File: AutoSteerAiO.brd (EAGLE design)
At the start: 114.3 x 99.1 mm, 84 parts, among them IC2 MMA8452Q, J4 CONNECTOR 1x5 PINS, K4 CB1A-P-12V, U1 VX7805-1000

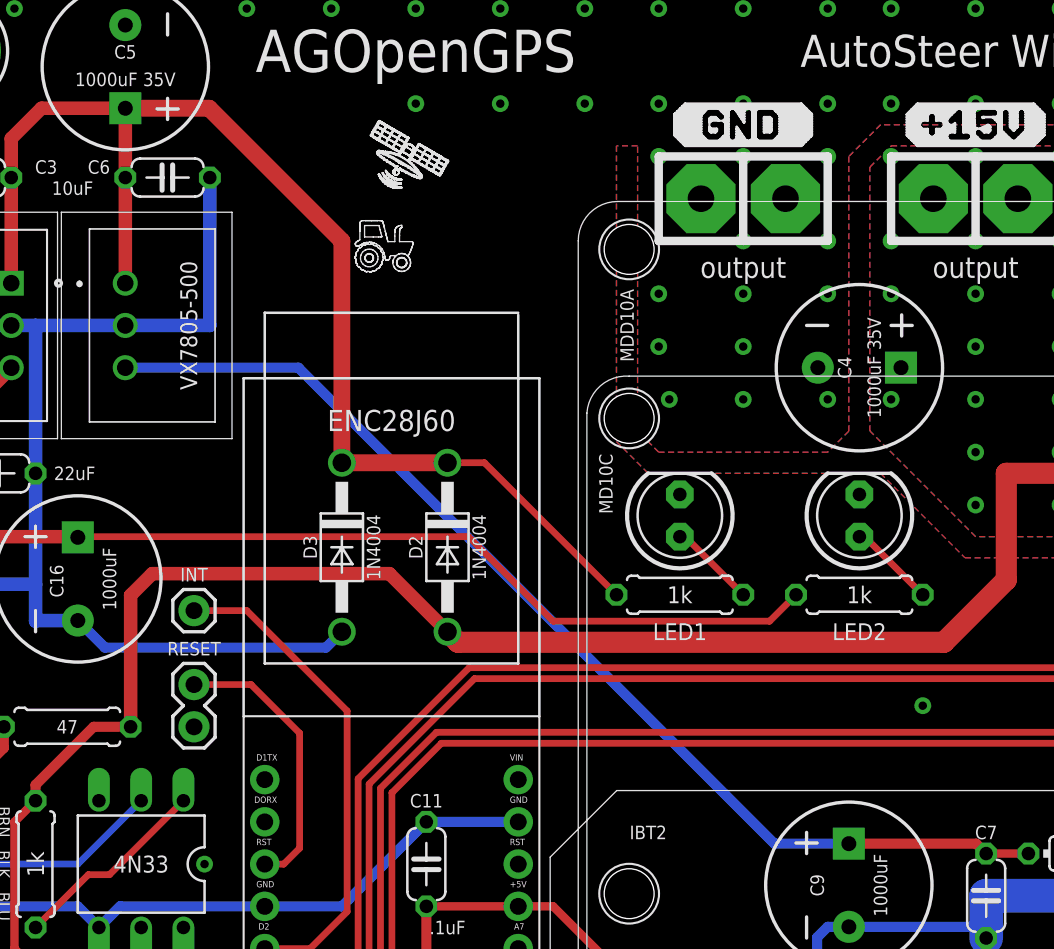
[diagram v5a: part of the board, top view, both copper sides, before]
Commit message: Add files via upload
previous version, wrong footprint VX7805-1000 it can fit, but will come out from PCB.
now it's fixed
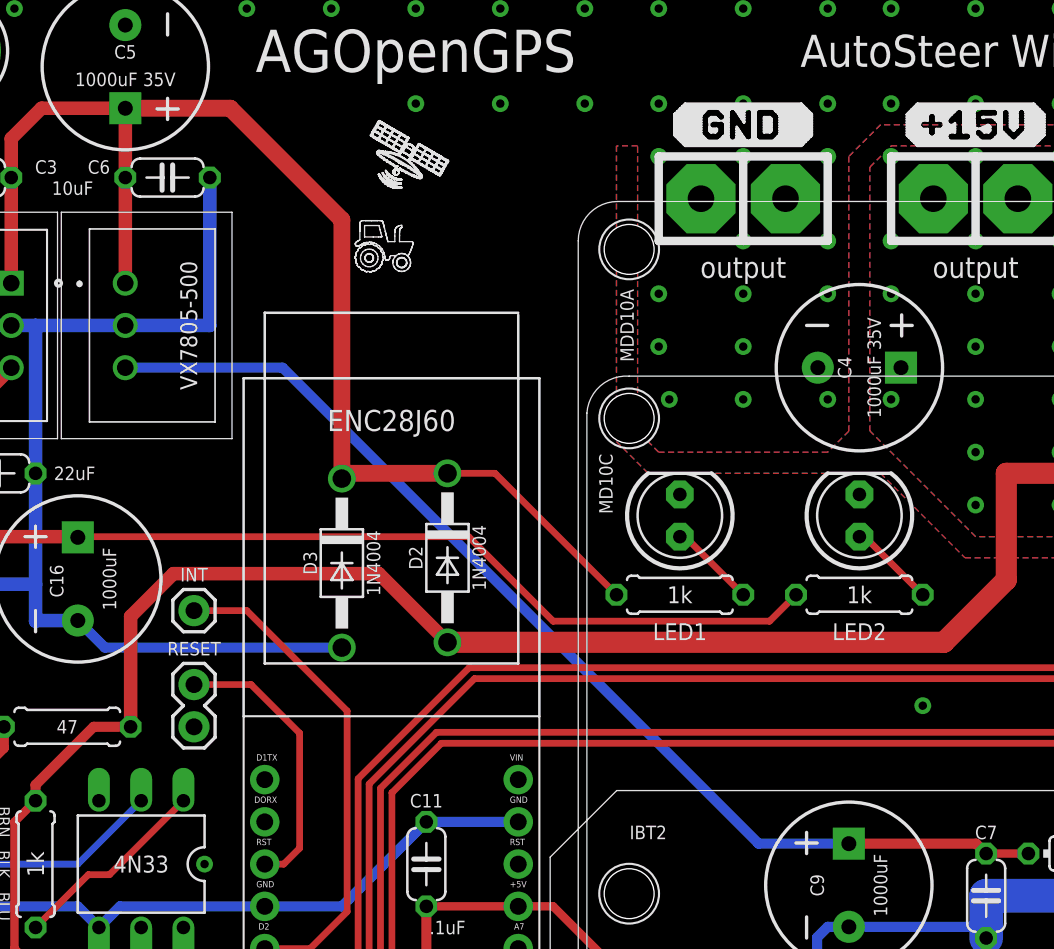
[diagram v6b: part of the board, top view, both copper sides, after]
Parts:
- moved D3 0.95 mm to (28.6, 63.2)
- moved D2 0.64 mm to (34.9, 63.5)
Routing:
- net N$26: track 76.3 -> 77.9 mm
- net +15V: track 121.6 -> 120.9 mm
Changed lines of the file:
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@@
 <?xml version="1.0" encoding="utf-8"?>
 <!DOCTYPE eagle SYSTEM "eagle.dtd">
-<eagle version="9.3.1">
+<eagle version="9.3.2">
 <drawing>
 <settings>
@@
 <attribute name="CYTRON-PC" value="CN-2600PS-05" x="109.855" y="48.26" size="1.778" layer="27" rot="R90" display="off"/>
 <attribute name="DESC" value="2600 PCB Connector" x="109.855" y="48.26" size="1.778" layer="27" rot="R90" display="off"/>
-<attribute name="LABEL" value="" x="112.776" y="46.863" size="0.762" layer="21" font="vector" ratio="15" rot="R90" align="top-left"/>
 <attribute name="LABEL" value="" x="112.776" y="46.863" size="0.762" layer="51" font="vector" ratio="15" rot="R90" align="top-left"/>
+<attribute name="LABEL" value="" x="112.776" y="46.863" size="0.762" layer="21" font="vector" ratio="15" rot="R90" align="top-left"/>
 <attribute name="LABEL" value="" x="109.855" y="48.26" size="1.778" layer="27" rot="R90" display="off"/>
 <attribute name="MF" value="" x="109.855" y="48.26" size="1.778" layer="27" rot="R90" display="off"/>
@@
 <attribute name="VALUE" x="16.51" y="6.985" size="1.016" layer="25" font="vector" ratio="12" rot="R180" align="center"/>
 </element>
-<element name="D2" library="diode" library_urn="urn:adsk.eagle:library:210" package="DO41-10" package3d_urn="urn:adsk.eagle:package:43336/1" value="1N4004" x="34.925" y="64.135" smashed="yes" rot="R270">
-<attribute name="MF" value="" x="34.925" y="64.135" size="1.778" layer="27" rot="R270" display="off"/>
-<attribute name="MPN" value="" x="34.925" y="64.135" size="1.778" layer="27" rot="R270" display="off"/>
-<attribute name="NAME" x="33.02" y="64.135" size="0.8128" layer="25" font="vector" ratio="12" rot="R90" align="center"/>
-<attribute name="OC_NEWARK" value="unknown" x="34.925" y="64.135" size="1.778" layer="27" rot="R270" display="off"/>
-<attribute name="VALUE" x="36.83" y="64.135" size="0.8128" layer="25" font="vector" ratio="12" rot="R90" align="center"/>
-</element>
-<element name="D3" library="diode" library_urn="urn:adsk.eagle:library:210" package="DO41-10" package3d_urn="urn:adsk.eagle:package:43336/1" value="1N4004" x="28.575" y="64.135" smashed="yes" rot="R270">
-<attribute name="MF" value="" x="28.575" y="64.135" size="1.778" layer="27" rot="R270" display="off"/>
-<attribute name="MPN" value="" x="28.575" y="64.135" size="1.778" layer="27" rot="R270" display="off"/>
-<attribute name="NAME" x="26.67" y="64.135" size="0.8128" layer="25" font="vector" ratio="12" rot="R270" align="center"/>
-<attribute name="OC_NEWARK" value="unknown" x="28.575" y="64.135" size="1.778" layer="27" rot="R270" display="off"/>
-<attribute name="VALUE" x="30.48" y="64.135" size="0.8128" layer="25" font="vector" ratio="12" rot="R270" align="center"/>
+<element name="D2" library="diode" library_urn="urn:adsk.eagle:library:210" package="DO41-10" package3d_urn="urn:adsk.eagle:package:43336/1" value="1N4004" x="34.925" y="63.5" smashed="yes" rot="R270">
+<attribute name="MF" value="" x="34.925" y="63.5" size="1.778" layer="27" rot="R270" display="off"/>
+<attribute name="MPN" value="" x="34.925" y="63.5" size="1.778" layer="27" rot="R270" display="off"/>
+<attribute name="NAME" x="33.02" y="63.5" size="0.8128" layer="25" font="vector" ratio="12" rot="R90" align="center"/>
+<attribute name="OC_NEWARK" value="unknown" x="34.925" y="63.5" size="1.778" layer="27" rot="R270" display="off"/>
+<attribute name="VALUE" x="36.83" y="63.5" size="0.8128" layer="25" font="vector" ratio="12" rot="R90" align="center"/>
+</element>
+<element name="D3" library="diode" library_urn="urn:adsk.eagle:library:210" package="DO41-10" package3d_urn="urn:adsk.eagle:package:43336/1" value="1N4004" x="28.575" y="63.1825" smashed="yes" rot="R270">
+<attribute name="MF" value="" x="28.575" y="63.1825" size="1.778" layer="27" rot="R270" display="off"/>
+<attribute name="MPN" value="" x="28.575" y="63.1825" size="1.778" layer="27" rot="R270" display="off"/>
+<attribute name="NAME" x="26.67" y="63.1825" size="0.8128" layer="25" font="vector" ratio="12" rot="R270" align="center"/>
+<attribute name="OC_NEWARK" value="unknown" x="28.575" y="63.1825" size="1.778" layer="27" rot="R270" display="off"/>
+<attribute name="VALUE" x="30.48" y="63.1825" size="0.8128" layer="25" font="vector" ratio="12" rot="R270" align="center"/>
 </element>
 <element name="R4" library="resistor" library_urn="urn:adsk.eagle:library:348" package="0207/7" package3d_urn="urn:adsk.eagle:package:23493/2" value="330" x="96.52" y="20.955" smashed="yes" rot="R180">
@@
 <via x="105.41" y="2.54" extent="1-16" drill="0.508"/>
 <via x="33.02" y="90.805" extent="1-16" drill="0.508"/>
-<wire x1="28.575" y1="59.055" x2="27.6225" y2="58.1025" width="0.6096" layer="16"/>
-<wire x1="27.6225" y1="58.1025" x2="14.3275" y2="58.1025" width="0.6096" layer="16"/>
+<wire x1="28.575" y1="58.1025" x2="14.3275" y2="58.1025" width="0.6096" layer="16"/>
 <wire x1="12.7" y1="59.73" x2="14.3275" y2="58.1025" width="0.6096" layer="16"/>
 <polygon width="0" layer="1" isolate="0.3556" thermals="no" rank="2">
@@
 <wire x1="8.89" y1="40.005" x2="8.89" y2="47.625" width="0.508" layer="1"/>
 <wire x1="8.89" y1="47.625" x2="10.16" y2="48.895" width="0.508" layer="1"/>
-<wire x1="34.925" y1="59.055" x2="31.4325" y2="62.5475" width="0.8128" layer="1"/>
-<wire x1="31.4325" y1="62.5475" x2="17.1763125" y2="62.5475" width="0.8128" layer="1"/>
-<wire x1="17.1763125" y1="62.5475" x2="15.875" y2="61.2461875" width="0.8128" layer="1"/>
+<wire x1="34.925" y1="58.42" x2="30.7975" y2="62.5475" width="0.8128" layer="1"/>
+<wire x1="30.7975" y1="62.5475" x2="18.4463125" y2="62.5475" width="0.8128" layer="1"/>
+<wire x1="18.4463125" y1="62.5475" x2="15.875" y2="59.9761875" width="0.8128" layer="1"/>
 <polygon width="0" layer="16" thermals="no">
 <vertex x="66.675" y="64.77"/>
@@
 <vertex x="79.375" y="64.77"/>
 </polygon>
-<wire x1="15.875" y1="61.2461875" x2="15.875" y2="53.34" width="0.8128" layer="1"/>
+<wire x1="15.875" y1="59.9761875" x2="15.875" y2="53.34" width="0.8128" layer="1"/>
 <wire x1="15.875" y1="53.34" x2="13.6525" y2="53.34" width="0.6096" layer="1"/>
 <wire x1="13.6525" y1="53.34" x2="10.16" y2="49.8475" width="0.6096" layer="1"/>
@@
 <via x="71.755" y="66.675" extent="1-16" drill="0.508"/>
 <via x="75.565" y="66.675" extent="1-16" drill="0.508"/>
-<wire x1="64.77" y1="58.42" x2="35.56" y2="58.42" width="1.27" layer="1"/>
-<wire x1="35.56" y1="58.42" x2="35.179" y2="58.801" width="1.27" layer="1"/>
-<wire x1="35.179" y1="58.801" x2="34.925" y2="59.055" width="1.27" layer="1"/>
+<wire x1="64.77" y1="58.42" x2="34.925" y2="58.42" width="1.27" layer="1"/>
 <wire x1="78.68" y1="68.58" x2="68.52" y2="68.58" width="1.27" layer="1"/>
 <wire x1="68.52" y1="68.58" x2="68.52" y2="62.17" width="1.27" layer="1"/>
@@
 <wire x1="15.5575" y1="80.01" x2="15.555" y2="80.0125" width="0.8128" layer="1"/>
 <wire x1="15.555" y1="80.0125" x2="15.5525" y2="80.01" width="0.8128" layer="1"/>
-<wire x1="34.925" y1="69.215" x2="37.1475" y2="69.215" width="0.4064" layer="1"/>
-<wire x1="45.085" y1="61.2775" x2="37.1475" y2="69.215" width="0.4064" layer="1"/>
+<wire x1="34.925" y1="68.58" x2="37.7825" y2="68.58" width="0.4064" layer="1"/>
+<wire x1="45.085" y1="61.2775" x2="37.7825" y2="68.58" width="0.4064" layer="1"/>
 <wire x1="15.5575" y1="90.5275" x2="15.5575" y2="86.36" width="0.8128" layer="1"/>
 <contactref element="U1" pad="1"/>
@@
 <wire x1="8.6995" y1="86.36" x2="8.7" y2="86.3595" width="0.8128" layer="1"/>
 <wire x1="8.7" y1="86.3595" x2="8.7" y2="80.01" width="0.8128" layer="1"/>
-<wire x1="34.925" y1="69.215" x2="28.575" y2="69.215" width="1.016" layer="1"/>
-<wire x1="28.575" y1="69.215" x2="28.575" y2="82.55" width="1.016" layer="1"/>
-<wire x1="20.5975" y1="90.5275" x2="15.5575" y2="90.5275" width="1.016" layer="1"/>
-<wire x1="28.575" y1="82.55" x2="20.5975" y2="90.5275" width="1.016" layer="1"/>
+<wire x1="34.925" y1="68.58" x2="28.8925" y2="68.58" width="1.016" layer="1"/>
+<wire x1="28.575" y1="68.2625" x2="28.8925" y2="68.58" width="1.016" layer="1"/>
+<wire x1="28.575" y1="68.2625" x2="28.575" y2="83.82" width="1.016" layer="1"/>
+<wire x1="21.8675" y1="90.5275" x2="15.5575" y2="90.5275" width="1.016" layer="1"/>
+<wire x1="28.575" y1="83.82" x2="21.8675" y2="90.5275" width="1.016" layer="1"/>
 </signal>
 <signal name="D2">
@@
 <wire x1="67.31" y1="45.72" x2="66.715" y2="46.315" width="0.6096" layer="1"/>
 <wire x1="66.715" y1="46.315" x2="59.055" y2="46.315" width="0.6096" layer="1"/>
-<wire x1="54.5815" y1="46.315" x2="25.9665" y2="74.93" width="0.6096" layer="16"/>
-<wire x1="15.5525" y1="74.93" x2="25.9665" y2="74.93" width="0.6096" layer="16"/>
-<wire x1="54.5815" y1="46.315" x2="59.055" y2="46.315" width="0.6096" layer="16"/>
+<wire x1="53.629" y1="46.315" x2="25.014" y2="74.93" width="0.6096" layer="16"/>
+<wire x1="15.5525" y1="74.93" x2="25.014" y2="74.93" width="0.6096" layer="16"/>
+<wire x1="53.629" y1="46.315" x2="59.055" y2="46.315" width="0.6096" layer="16"/>
 </signal>
 <signal name="N$3">

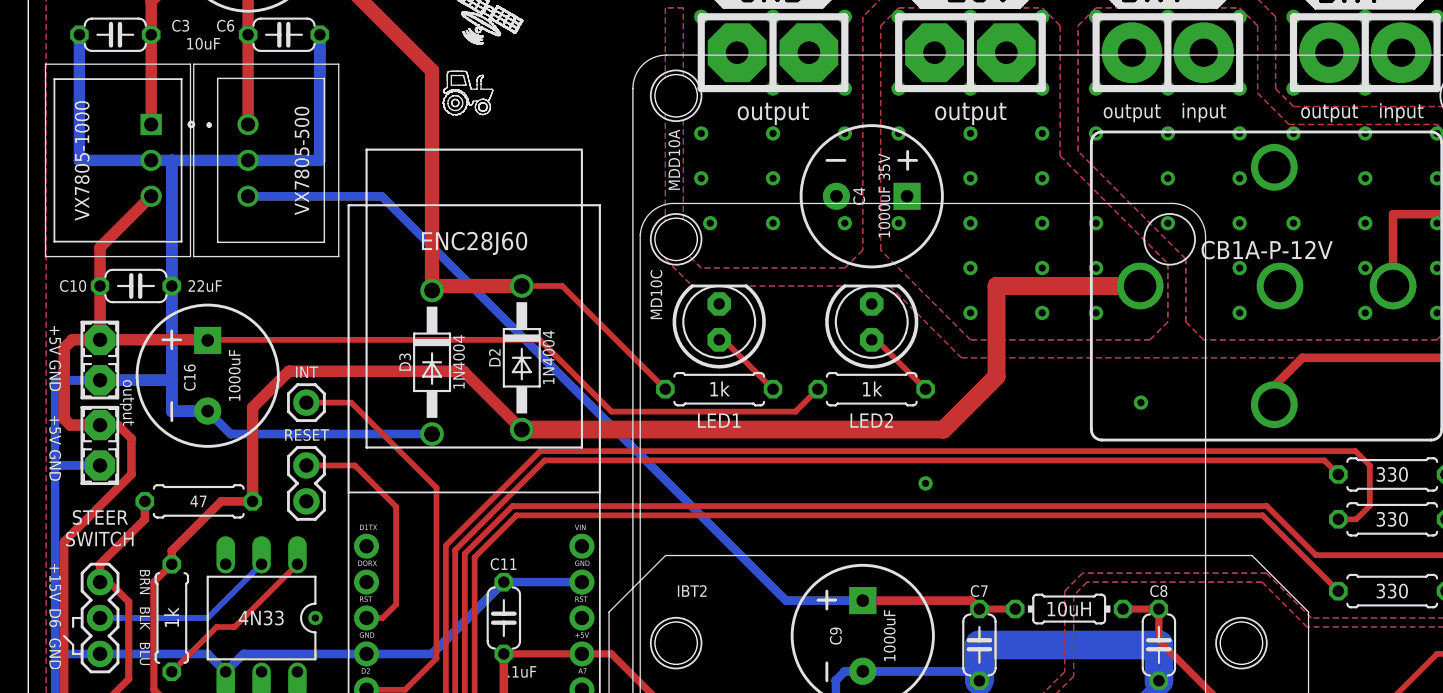
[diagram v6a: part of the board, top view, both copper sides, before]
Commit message: Add files via upload
edit silkscreen
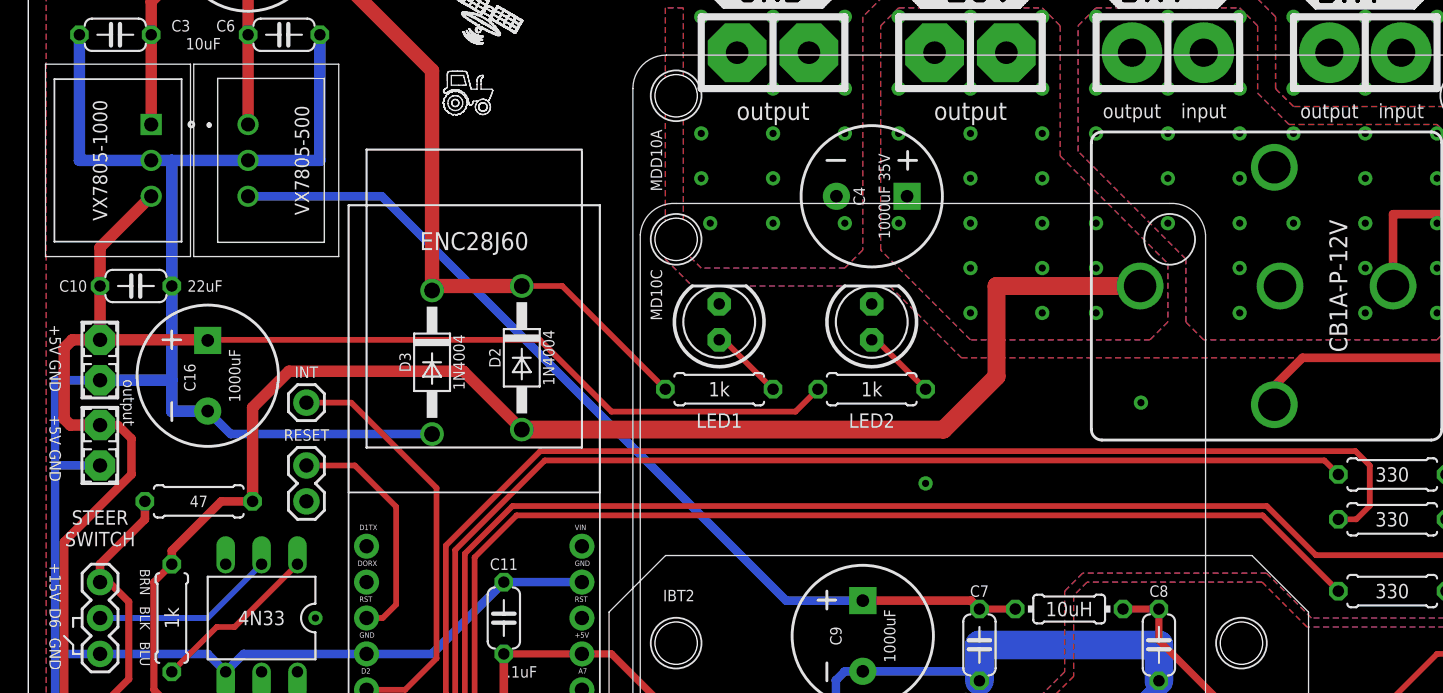
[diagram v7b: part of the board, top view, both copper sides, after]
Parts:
- moved U$11 2.54 mm to (74.3, 58.4)
- moved U$12 2.54 mm to (75.6, 52.7)
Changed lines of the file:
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@@
 <drawing>
 <settings>
-<setting alwaysvectorfont="no"/>
+<setting alwaysvectorfont="yes"/>
 <setting keepoldvectorfont="yes"/>
 <setting verticaltext="up"/>
@@
 <text x="107.95" y="13.335" size="0.7112" layer="25" font="vector" ratio="15" rot="R270" align="center">GND</text>
 <text x="97.155" y="2.54" size="0.8128" layer="25" font="vector" ratio="14" rot="R180" align="center">MD13S</text>
-<text x="46.99" y="46.99" size="0.8128" layer="25" font="vector" ratio="14" rot="R180" align="center">IBT2</text>
-<text x="45.72" y="77.47" size="0.8128" layer="25" font="vector" ratio="14" rot="R90" align="center">MDD10A</text>
+<text x="46.0375" y="46.6725" size="0.8128" layer="25" font="vector" ratio="14" rot="R180" align="center">IBT2</text>
+<text x="44.45" y="77.47" size="0.8128" layer="25" font="vector" ratio="14" rot="R90" align="center">MDD10A</text>
 <text x="1.905" y="58.42" size="0.8128" layer="25" font="vector" ratio="14" rot="SR270" align="center">+5V</text>
 <text x="1.905" y="55.88" size="0.8128" layer="25" font="vector" ratio="14" rot="SR270" align="center">GND</text>
@@
 <text x="40.9575" y="3.175" size="0.8128" layer="26" font="vector" ratio="14" rot="MR270" align="center">MDD10A</text>
 <text x="103.8225" y="81.915" size="0.8128" layer="26" font="vector" ratio="14" rot="MR270" align="center">MDD10A</text>
-<text x="3.81" y="77.47" size="1.016" layer="25" font="vector" ratio="14" rot="R270" align="center">VX7805-1000</text>
+<text x="5.08" y="77.47" size="1.016" layer="25" font="vector" ratio="14" rot="R270" align="center">VX7805-1000</text>
 </plain>
 <attributes>
@@
 <attribute name="CYTRON-PC" value="CN-2600PS-05" x="109.855" y="48.26" size="1.778" layer="27" rot="R90" display="off"/>
 <attribute name="DESC" value="2600 PCB Connector" x="109.855" y="48.26" size="1.778" layer="27" rot="R90" display="off"/>
+<attribute name="LABEL" value="" x="112.776" y="46.863" size="0.762" layer="21" font="vector" ratio="15" rot="R90" align="top-left"/>
 <attribute name="LABEL" value="" x="112.776" y="46.863" size="0.762" layer="51" font="vector" ratio="15" rot="R90" align="top-left"/>
-<attribute name="LABEL" value="" x="112.776" y="46.863" size="0.762" layer="21" font="vector" ratio="15" rot="R90" align="top-left"/>
 <attribute name="LABEL" value="" x="109.855" y="48.26" size="1.778" layer="27" rot="R90" display="off"/>
 <attribute name="MF" value="" x="109.855" y="48.26" size="1.778" layer="27" rot="R90" display="off"/>
@@
 <attribute name="OC_FARNELL" value="1270582" x="87.63" y="68.58" size="1.778" layer="27" rot="R180" display="off"/>
 <attribute name="OC_NEWARK" value="unknown" x="87.63" y="68.58" size="1.778" layer="27" rot="R180" display="off"/>
-<attribute name="VALUE" x="87.63" y="71.12" size="1.27" layer="25" font="vector" ratio="14" rot="R180" align="center"/>
+<attribute name="VALUE" x="92.71" y="68.58" size="1.27" layer="25" font="vector" ratio="14" rot="R270" align="center"/>
 </element>
 <element name="OK2" library="optocoupler" library_urn="urn:adsk.eagle:library:320" package="DIL06" package3d_urn="urn:adsk.eagle:package:21942/1" value="4N33" x="16.51" y="29.845" smashed="yes" rot="R180">
@@
 <attribute name="OC_NEWARK" value="90Y6375" x="45.847" y="3.302" size="1.778" layer="27" rot="R90" display="off"/>
 </element>
-<element name="U$11" library="#Logo" package="SATELIT-MALI" value="SATELIT-MALI" x="71.755" y="58.42" smashed="yes" rot="MR0">
-<attribute name="MF" value="" x="71.755" y="58.42" size="1.778" layer="28" rot="MR0" display="off"/>
-<attribute name="MPN" value="" x="71.755" y="58.42" size="1.778" layer="28" rot="MR0" display="off"/>
-<attribute name="OC_NEWARK" value="unknown" x="71.755" y="58.42" size="1.778" layer="28" rot="MR0" display="off"/>
-</element>
-<element name="U$12" library="#Logo" package="TRAKTOR-MALI" value="TRAKTOR-MALI" x="73.025" y="52.705" smashed="yes" rot="MR0">
-<attribute name="MF" value="" x="73.025" y="52.705" size="1.778" layer="28" rot="MR0" display="off"/>
-<attribute name="MPN" value="" x="73.025" y="52.705" size="1.778" layer="28" rot="MR0" display="off"/>
-<attribute name="OC_NEWARK" value="unknown" x="73.025" y="52.705" size="1.778" layer="28" rot="MR0" display="off"/>
+<element name="U$11" library="#Logo" package="SATELIT-MALI" value="SATELIT-MALI" x="74.295" y="58.42" smashed="yes" rot="MR0">
+<attribute name="MF" value="" x="74.295" y="58.42" size="1.778" layer="28" rot="MR0" display="off"/>
+<attribute name="MPN" value="" x="74.295" y="58.42" size="1.778" layer="28" rot="MR0" display="off"/>
+<attribute name="OC_NEWARK" value="unknown" x="74.295" y="58.42" size="1.778" layer="28" rot="MR0" display="off"/>
+</element>
+<element name="U$12" library="#Logo" package="TRAKTOR-MALI" value="TRAKTOR-MALI" x="75.565" y="52.705" smashed="yes" rot="MR0">
+<attribute name="MF" value="" x="75.565" y="52.705" size="1.778" layer="28" rot="MR0" display="off"/>
+<attribute name="MPN" value="" x="75.565" y="52.705" size="1.778" layer="28" rot="MR0" display="off"/>
+<attribute name="OC_NEWARK" value="unknown" x="75.565" y="52.705" size="1.778" layer="28" rot="MR0" display="off"/>
 </element>
 <element name="U1" library="#VX7805-1000" package="VX78012-1000_VX7805-1000" value="VX7805-1000" x="6.35" y="77.47" smashed="yes" rot="R270">
